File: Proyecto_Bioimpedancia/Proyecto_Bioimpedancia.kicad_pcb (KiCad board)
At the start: 2 copper layers, 53 parts, among them J1 Jumper_Calibration, J2 Jumper, J3 Jumper, J4 Jumper, P1 CONN_01X05, P2 CONN_01X02, P3 CONN_01X02, P4 CONN_01X02, SW1 SW_PUSH, U1 AD8606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

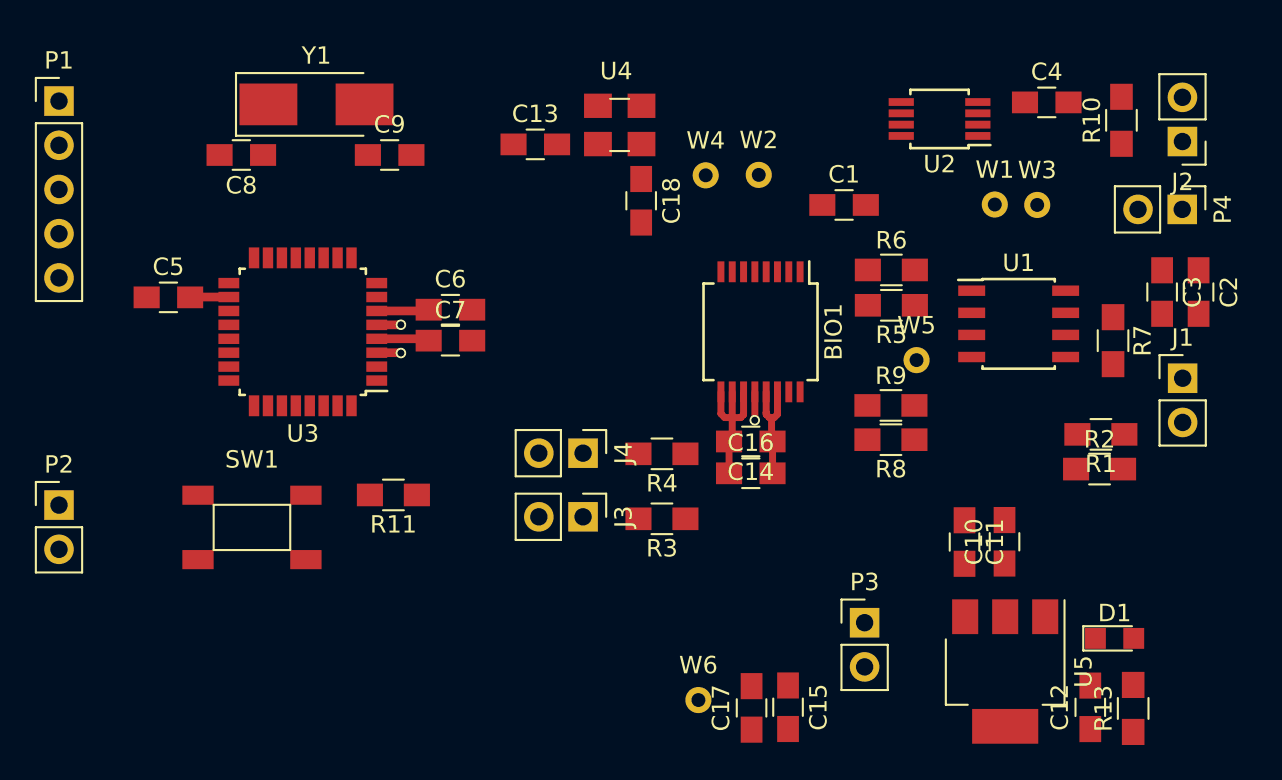
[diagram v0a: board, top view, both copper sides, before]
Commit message: Layout casi terminado
Faltan tierras y polarización solamente
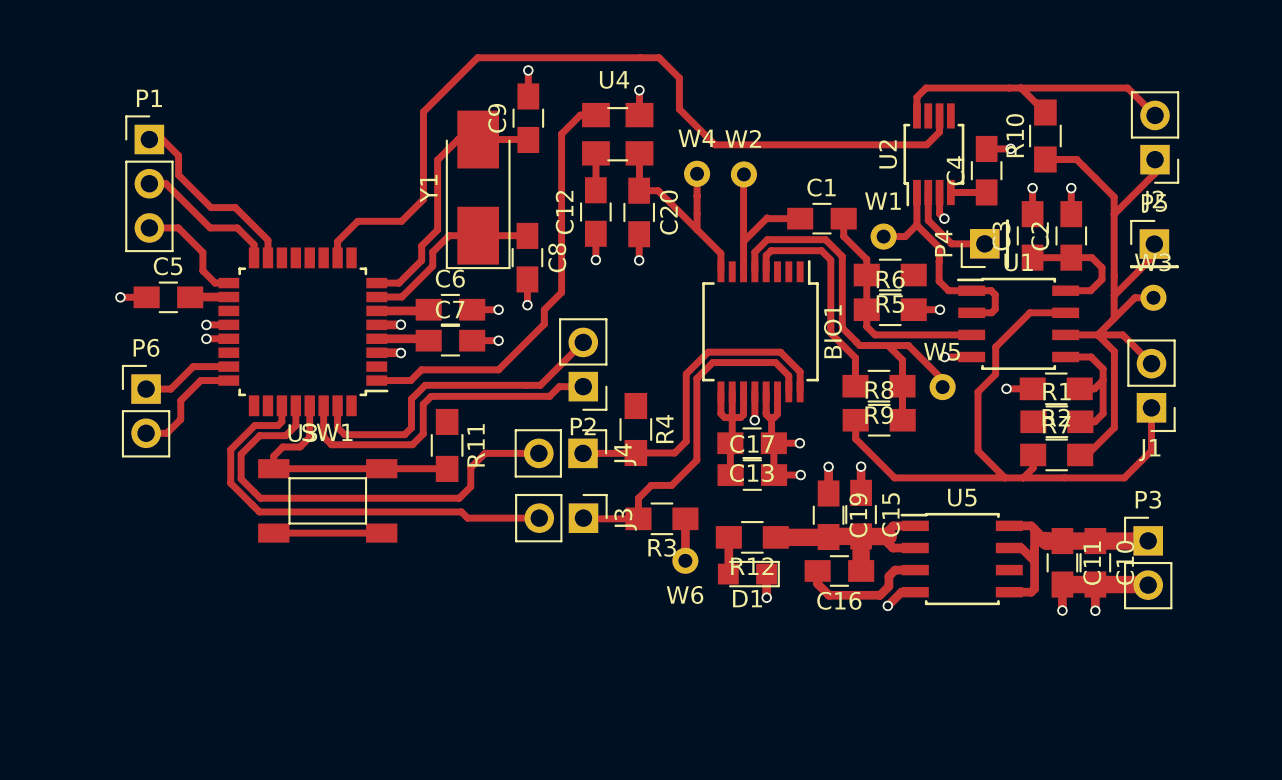
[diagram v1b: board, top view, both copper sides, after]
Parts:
- removed C14: 0,1uF, Capacitors_SMD:C_0805_HandSoldering
- removed C18: 20pF, Capacitors_SMD:C_0805_HandSoldering
- removed R13: 1K, Resistors_SMD:R_0805_HandSoldering
- added C19: 10uF, Capacitors_SMD:C_0805_HandSoldering, F.Cu at (216.3, 78.8)
- added C20: 20pF, Capacitors_SMD:C_0805_HandSoldering, F.Cu at (205.4, 61.4)
- added P5: CONN_01X01, Socket_Strips:Socket_Strip_Straight_1x01_Pitch2.54mm, F.Cu at (235.0, 63.2)
- added P6: CONN_01X02, Socket_Strips:Socket_Strip_Straight_1x02_Pitch2.54mm, F.Cu at (177.1, 71.6)
- added R12: 1K, Resistors_SMD:R_0805_HandSoldering, F.Cu at (211.9, 80.1)
- C10: value 1uF -> 0,1uF
- C11: value 1uF -> 10uF
- C12: value 1uF -> 0,01uF
- C13: value 0,01uF -> 0,1uF
- C16: value 10uF -> 0,1uF
- P1: value CONN_01X05 -> CONN_01X03; footprint Socket_Strips:Socket_Strip_Straight_1x05_Pitch2.54mm -> Socket_Strips:Socket_Strip_Straight_1x03_Pitch2.54mm
- P4: value CONN_01X02 -> CONN_01X01; footprint Socket_Strips:Socket_Strip_Straight_1x02_Pitch2.54mm -> Socket_Strips:Socket_Strip_Straight_1x01_Pitch2.54mm
- U5: value ADP3339 -> ADP3303; footprint TO_SOT_Packages_SMD:SOT-223 -> Housings_SOIC:SOIC-8_3.9x4.9mm_Pitch1.27mm
- moved C12 40.2 mm to (202.9, 61.4)
- moved P2 30.9 mm to (202.2, 71.4), turned to 180 degrees
- moved D1 21.4 mm to (211.6, 82.2), turned to 180 degrees
- moved C13 21.2 mm to (211.9, 74.7), turned to 180 degrees
- moved C8 17.5 mm to (199.0, 64.0), turned to 270 degrees
- moved P3 17.0 mm to (234.7, 80.3)
- moved C17 13.4 mm to (211.9, 76.5), turned to 0 degrees
- moved C15 11.8 mm to (218.2, 78.8)
- moved P4 11.5 mm to (225.3, 63.2), turned to 90 degrees
- moved Y1 10.4 mm to (196.2, 60.0), turned to 90 degrees
- moved W3 8.55 mm to (235.0, 66.3)
- moved C9 8.25 mm to (199.1, 56.0), turned to 90 degrees
- moved C3 8.11 mm to (228.0, 62.8), turned to 90 degrees
- moved W6 8.04 mm to (208.1, 81.4), turned to 180 degrees
- moved C2 7.99 mm to (230.3, 62.8), turned to 90 degrees
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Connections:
- C10 pad 1: /3V3 -> /V_FUENTE
- C11 pad 1: /AGND -> /V_FUENTE
- C11 pad 2: /V_FUENTE -> /AGND
- C12 pad 1: /3V3 -> /AGND
- C12 pad 2: /AGND -> /3V3
- C16 pad 2: /AGND -> Net-(C16-Pad2)
- U3 pad 1: (no net) -> /CTRL_MCLK
- U3 pad 10: (no net) -> /CTRL_SWITCH
- U3 pad 25: /CTRL_SWITCH -> (no net)
- U3 pad 26: /CTRL_MCLK -> (no net)
- U5 pad 1: /AGND -> /3V3
- U5 pad 3: /V_FUENTE -> Net-(C16-Pad2)
- U5 pad 4: /3V3 -> /AGND
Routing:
- net /AGND: track 11.1 -> 59.8 mm, vias 3 -> 28
- net /CTRL_SWITCH: track 0.00 -> 47.2 mm
- net /SIGNAL_A2: track 0.00 -> 38.3 mm
- net /FEEDBACK_A2: track 0.00 -> 37.1 mm
- net /3V3: track 17.3 -> 44.0 mm
- net Net-(J4-Pad2): track 0.00 -> 25.7 mm
- net Net-(J3-Pad2): track 0.00 -> 25.1 mm
- net /CTRL_MCLK: track 0.00 -> 24.7 mm
- net /VIN_AD5933: track 0.00 -> 23.1 mm
- net /SDA: track 0.00 -> 20.2 mm
- net /RXD: track 0.00 -> 19.3 mm
- net /SCL: track 0.00 -> 18.8 mm
- net /TXD: track 0.00 -> 18.7 mm
- net Net-(J2-Pad2): track 0.00 -> 17.6 mm
- net /V_FUENTE: track 0.00 -> 15.1 mm
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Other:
- net class Default: clearance 0.2 -> 0.1778; trace_width 0.25 -> 0.1778
- rule trace_clearance: 0.2 -> 0.1778
- rule trace_min: 0.2 -> 0.1524
- rule via_min_size: 0.4 -> 0.5

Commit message: PCB Final
Falta ultima revisión Esquematico
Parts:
- moved P1 8.18 mm to (185.5, 57.0), turned to 270 degrees
- moved P6 6.99 mm to (179.7, 78.1), turned to 180 degrees
- moved C5 1.48 mm to (179.2, 67.5), turned to 90 degrees
- moved C3 1.12 mm to (229.1, 62.7)
- moved C2 0.84 mm to (231.1, 62.7)
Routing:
- net /3V3: track 44.0 -> 199.0 mm, vias 0 -> 20
- net /ADC0: track 5.29 -> 12.7 mm
- net /AGND: track 59.8 -> 64.1 mm, vias 28 -> 30
- net /MOSI: track 10.9 -> 7.58 mm
- net /SCK: track 6.49 -> 9.55 mm
- net /MISO: track 8.22 -> 7.17 mm
- added copper zone on F.Cu, net /3V3
- added copper zone on B.Cu, net /AGND
- added copper zone on F.Cu, net /AGND
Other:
- board outline added: 61 x 33.3 mm

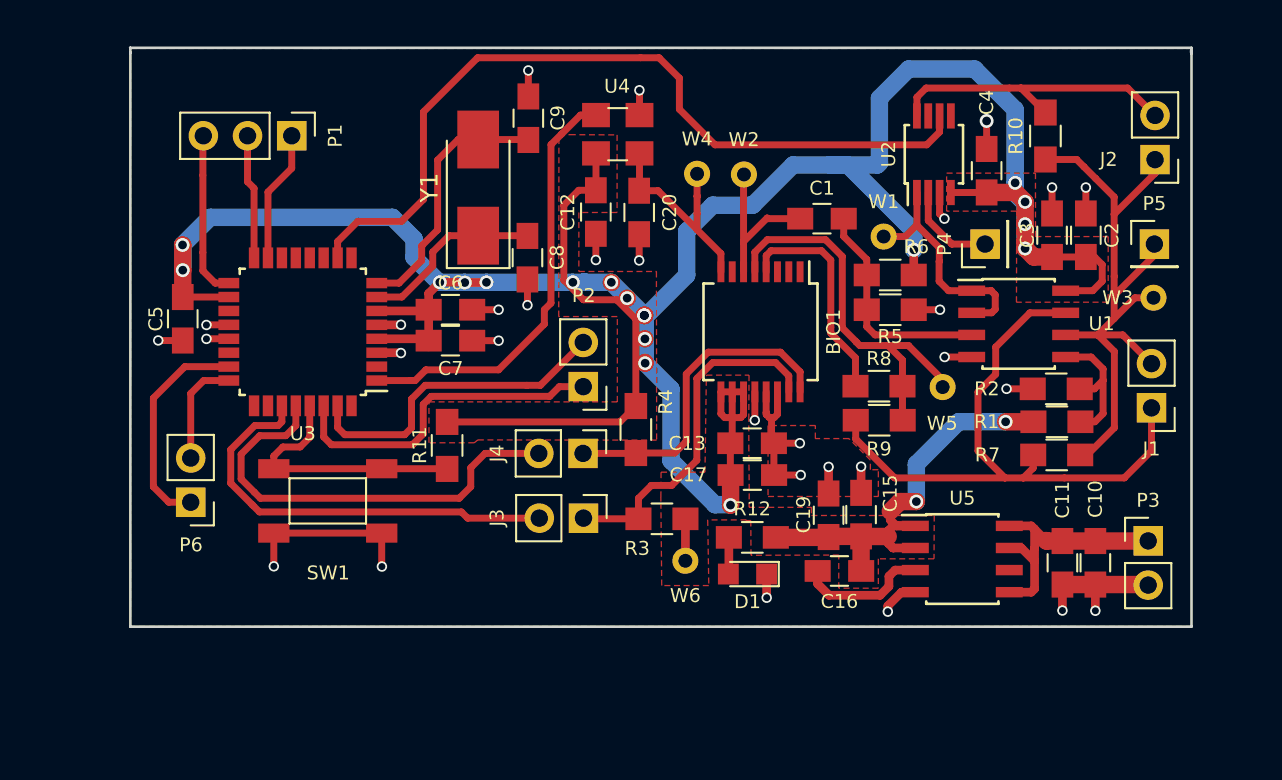
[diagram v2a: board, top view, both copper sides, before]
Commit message: Isletas añadidas a PCB
Revisar isletas
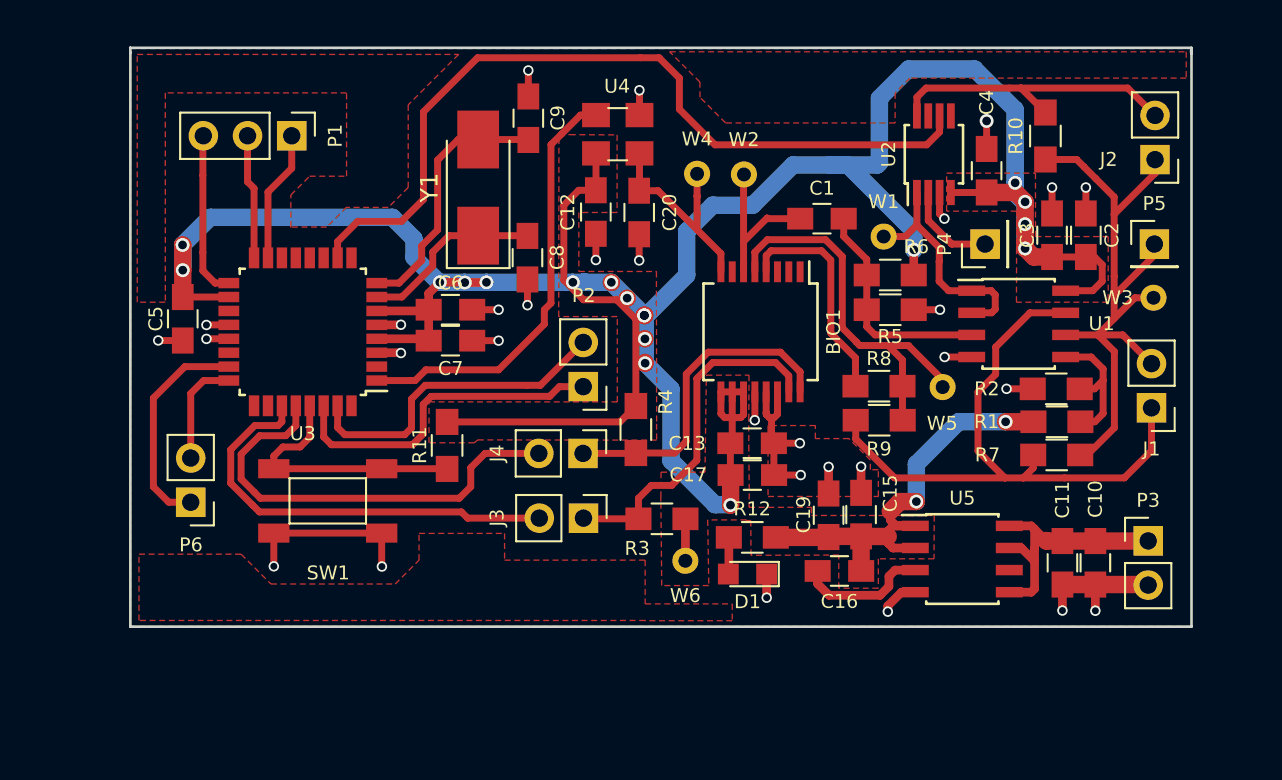
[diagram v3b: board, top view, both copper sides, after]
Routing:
- added copper zone on F.Cu, net (none)
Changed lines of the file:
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@@
   (layers
     (0 F.Cu signal)
-    (31 B.Cu signal)
+    (31 B.Cu signal hide)
     (32 B.Adhes user)
     (33 F.Adhes user)
@@
   )
   (setup
-    (last_trace_width 1)
+    (last_trace_width 0.1778)
     (user_trace_width 0.4)
     (user_trace_width 0.5)
@@
       )
     )
+  )
+  (zone (net 0) (net_name "") (layer F.Cu) (hatch edge 0.508)
+    (connect_pads (clearance 0.508))
+    (min_thickness 0.254)
+    (fill yes (arc_segments 16) (thermal_gap 0.508) (thermal_bridge_width 0.508))
+    (polygon
+      (pts
+        (xy 197.6882 81.3943) (xy 205.7654 81.3943) (xy 205.7654 83.9089) (xy 210.7692 83.9089) (xy 210.7692 84.8741)
+        (xy 205.7654 84.8741) (xy 205.765202 84.8614) (xy 176.6824 84.8614) (xy 176.6824 81.0514) (xy 182.5498 81.0514)
+        (xy 184.2643 82.7659) (xy 191.4017 82.7659) (xy 192.7733 81.3943) (xy 192.7733 79.8576) (xy 197.6882 79.8576)
+        (xy 197.6882 81.3943)
+      )
+    )
+  )
+  (zone (net 0) (net_name "") (layer F.Cu) (hatch edge 0.508)
+    (connect_pads (clearance 0.508))
+    (min_thickness 0.254)
+    (fill yes (arc_segments 16) (thermal_gap 0.508) (thermal_bridge_width 0.508))
+    (polygon
+      (pts
+        (xy 236.855 53.6956) (xy 220.98 53.6956) (xy 220.1291 54.5465) (xy 220.1291 56.2737) (xy 210.3882 56.2737)
+        (xy 208.915 54.8005) (xy 208.915 53.9242) (xy 207.1751 52.1843) (xy 236.855 52.1843) (xy 236.855 53.6956)
+      )
+    )
+  )
+  (zone (net 0) (net_name "") (layer F.Cu) (hatch edge 0.508)
+    (connect_pads (clearance 0.508))
+    (min_thickness 0.254)
+    (fill yes (arc_segments 16) (thermal_gap 0.508) (thermal_bridge_width 0.508))
+    (polygon
+      (pts
+        (xy 192.151 55.2323) (xy 192.151 59.9821) (xy 191.008 61.1251) (xy 188.6077 61.1251) (xy 188.6077 61.1124)
+        (xy 187.4647 62.2554) (xy 185.4073 62.2554) (xy 185.4073 60.4139) (xy 186.4868 59.3344) (xy 188.6077 59.3344)
+        (xy 188.6077 54.5465) (xy 178.1937 54.5465) (xy 178.1937 66.5734) (xy 176.5808 66.5734) (xy 176.5808 52.3367)
+        (xy 195.0466 52.3367) (xy 192.151 55.2323)
+      )
+    )
+  )
+  (zone (net 0) (net_name "") (layer F.Cu) (hatch edge 0.508)
+    (connect_pads (clearance 0.508))
+    (min_thickness 0.254)
+    (fill yes (arc_segments 16) (thermal_gap 0.508) (thermal_bridge_width 0.508))
+    (polygon
+      (pts
+        (xy 185.3946 62.2681) (xy 185.3946 62.2554) (xy 185.4073 62.2554) (xy 185.3946 62.2681)
+      )
+    )

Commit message: VersionFinal 2.0
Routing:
- net /3V3: vias 20 -> 19
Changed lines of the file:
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@@
     (thickness 1.6)
     (drawings 9)
-    (tracks 552)
+    (tracks 555)
     (zones 0)
     (modules 55)
@@
   )
   (setup
-    (last_trace_width 0.1778)
+    (last_trace_width 0.4)
     (user_trace_width 0.4)
     (user_trace_width 0.5)
@@
   (segment (start 205.4406 58.0214) (end 205.4406 60.1491) (width 0.4) (layer F.Cu) (net 4))
   (segment (start 205.4406 60.1491) (end 205.4225 60.1672) (width 0.4) (layer F.Cu) (net 4))
+  (segment (start 201.6125 65.4304) (end 196.6468 65.4304) (width 1) (layer B.Cu) (net 5))
   (segment (start 216.3699 58.6867) (end 217.4113 58.6867) (width 1) (layer B.Cu) (net 5))
   (segment (start 221.1997 63.5724) (end 221.1997 65.0113) (width 0.5) (layer F.Cu) (net 5))
@@
   (segment (start 195.4022 65.4304) (end 195.4022 65.4431) (width 0.5) (layer B.Cu) (net 5))
   (segment (start 195.4022 65.4431) (end 195.4022 65.4304) (width 0.5) (layer B.Cu) (net 5))
-  (via (at 201.6125 65.4304) (size 0.8) (drill 0.5) (layers F.Cu B.Cu) (net 5))
-  (segment (start 201.6125 65.4304) (end 196.6468 65.4304) (width 1) (layer B.Cu) (net 5))
   (segment (start 202.2729 65.4304) (end 201.6125 65.4304) (width 1) (layer B.Cu) (net 5))
   (segment (start 202.2729 65.405) (end 202.2729 65.4304) (width 1) (layer B.Cu) (net 5))
@@
   (segment (start 190.3431 68.6752) (end 193.2187 68.6752) (width 0.5) (layer F.Cu) (net 5))
   (segment (start 190.3431 67.0752) (end 193.2567 67.0752) (width 0.5) (layer F.Cu) (net 5))
+  (via (at 199.00265 67.1449) (size 0.6) (drill 0.4) (layers F.Cu B.Cu) (net 6))
+  (segment (start 199.00265 67.1449) (end 199.009 67.1449) (width 0.4) (layer B.Cu) (net 6))
+  (segment (start 199.00265 66.74485) (end 199.00265 67.1449) (width 0.4) (layer F.Cu) (net 6))
+  (segment (start 199.00265 67.1449) (end 199.00265 67.15125) (width 0.4) (layer F.Cu) (net 6))
+  (segment (start 199.00265 65.26435) (end 199.00265 66.74485) (width 0.4) (layer F.Cu) (net 6))
+  (segment (start 199.00265 67.15125) (end 198.9963 67.1576) (width 0.4) (layer F.Cu) (net 6))
   (segment (start 225.3869 57.7669) (end 225.3869 56.1594) (width 0.4) (layer F.Cu) (net 6))
   (via (at 225.3869 56.1594) (size 0.8) (drill 0.5) (layers F.Cu B.Cu) (net 6))
@@
   (via (at 214.6554 74.676) (size 0.6) (drill 0.4) (layers F.Cu B.Cu) (net 6))
   (segment (start 199.05345 54.75065) (end 199.05345 53.25745) (width 0.4) (layer F.Cu) (net 6))
-  (segment (start 199.00265 65.26435) (end 199.00265 66.74485) (width 0.4) (layer F.Cu) (net 6))
-  (via (at 199.00265 66.74485) (size 0.6) (drill 0.4) (layers F.Cu B.Cu) (net 6))
   (segment (start 181.8431 67.8752) (end 180.5622 67.8752) (width 0.4) (layer F.Cu) (net 6))
   (via (at 180.5559 67.8815) (size 0.6) (drill 0.4) (layers F.Cu B.Cu) (net 6))

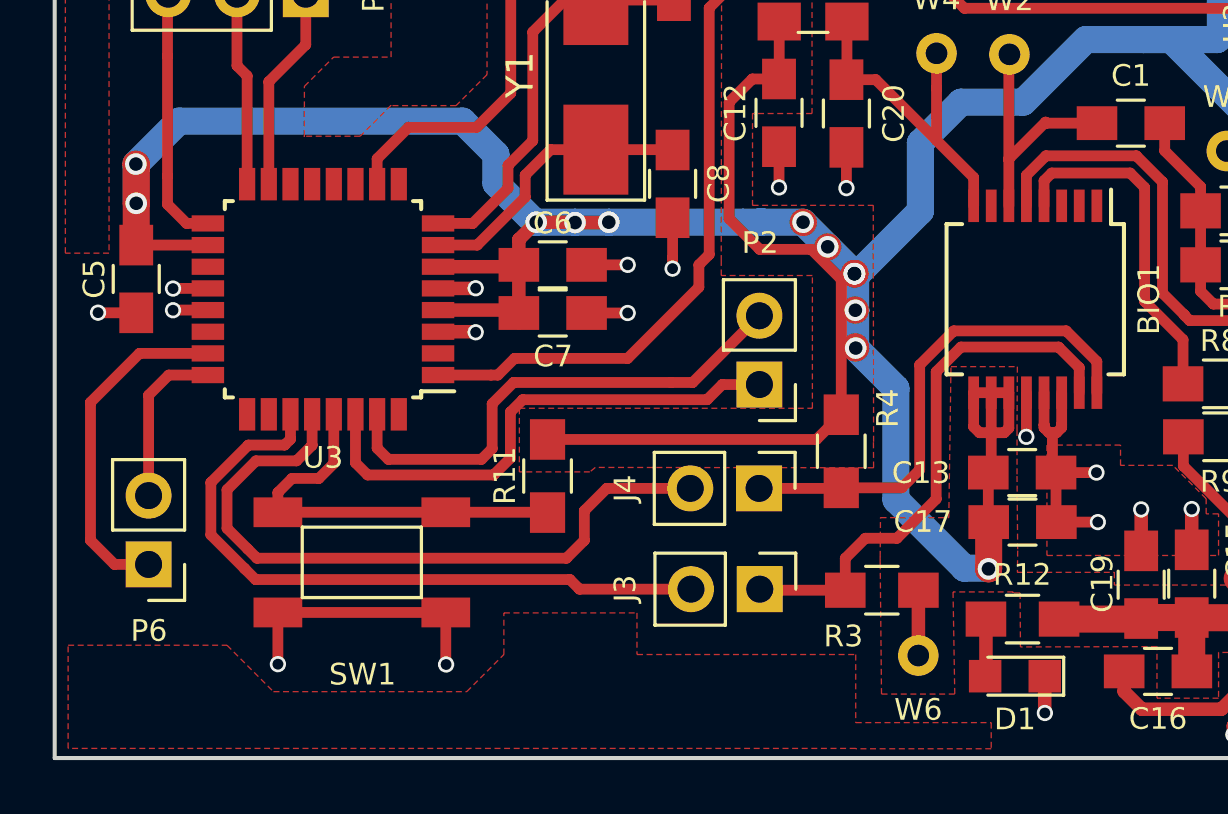
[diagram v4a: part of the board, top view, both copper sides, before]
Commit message: Version con BOM File aprobado
Falta solo la RAM
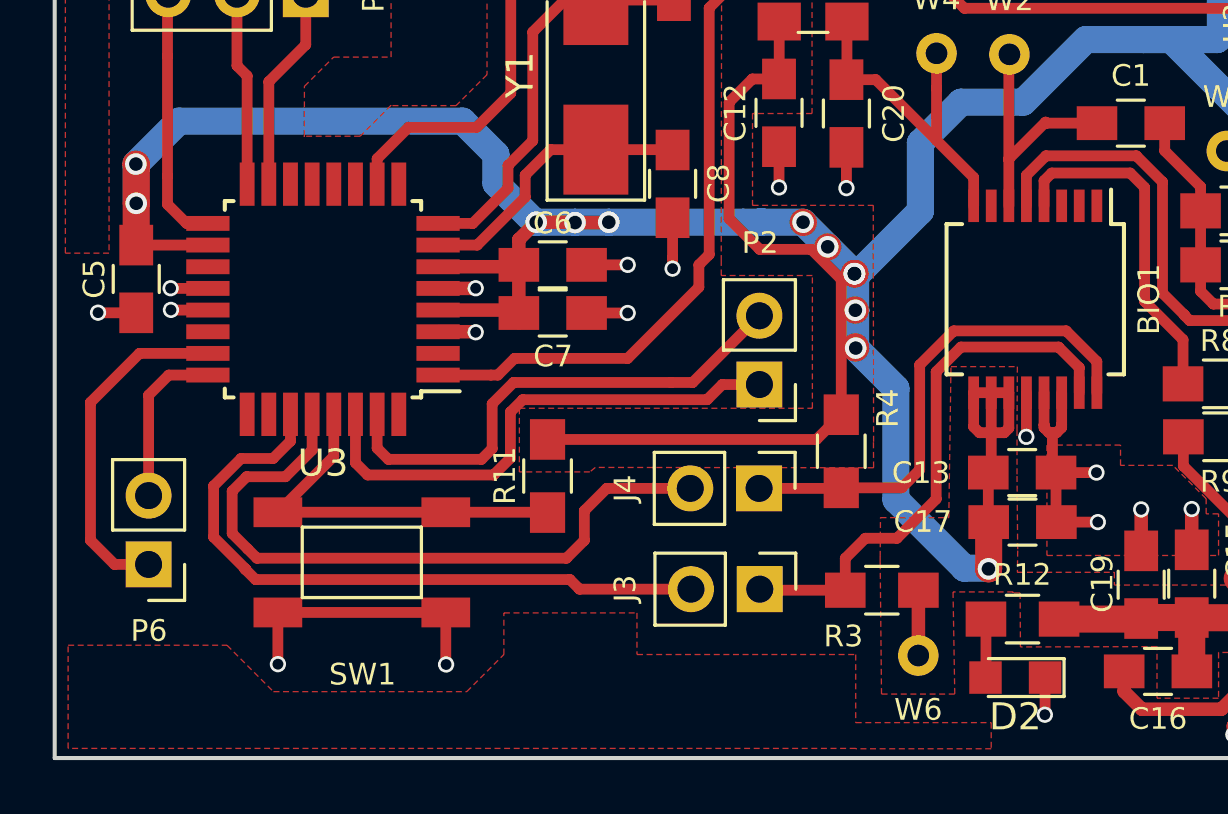
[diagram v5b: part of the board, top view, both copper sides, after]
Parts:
- removed D1: Led_Small, LEDs:LED_0805
- added D2: Led_Small_Reg, LEDs:LED_0805, F.Cu at (211.7, 82.2)
- C8, C9: value 22pF -> 18pF
- U3: footprint Housings_QFP:LQFP-32_7x7mm_Pitch0.8mm -> Housings_QFP:TQFP-32_7x7mm_Pitch0.8mm
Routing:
- net /RESET: track 15.0 -> 14.4 mm
